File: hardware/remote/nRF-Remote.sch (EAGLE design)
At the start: 26 parts, among them IC1 TP4056, IC2 TPS769XX, J1 62000611121, J2 61300211121, M1 WIRELESS-NRF24L01, SW1 B3F-1000, U1 ATMEGA328P-AU

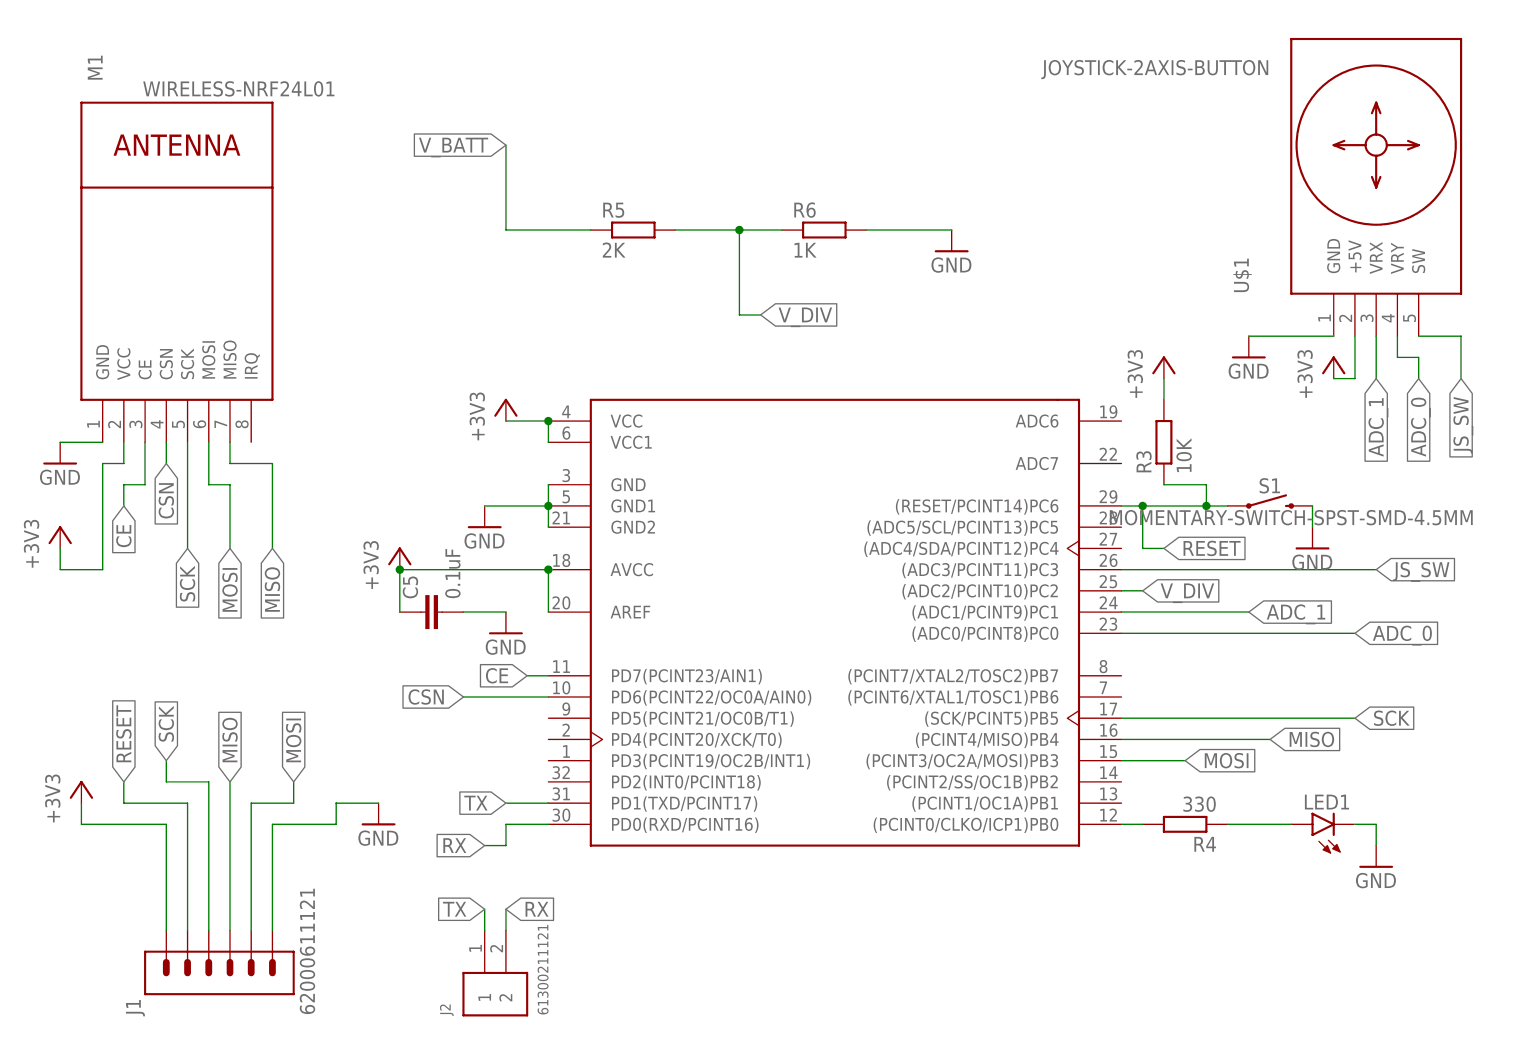
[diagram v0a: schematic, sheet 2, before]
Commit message: Update design with external XTAL, add buttons
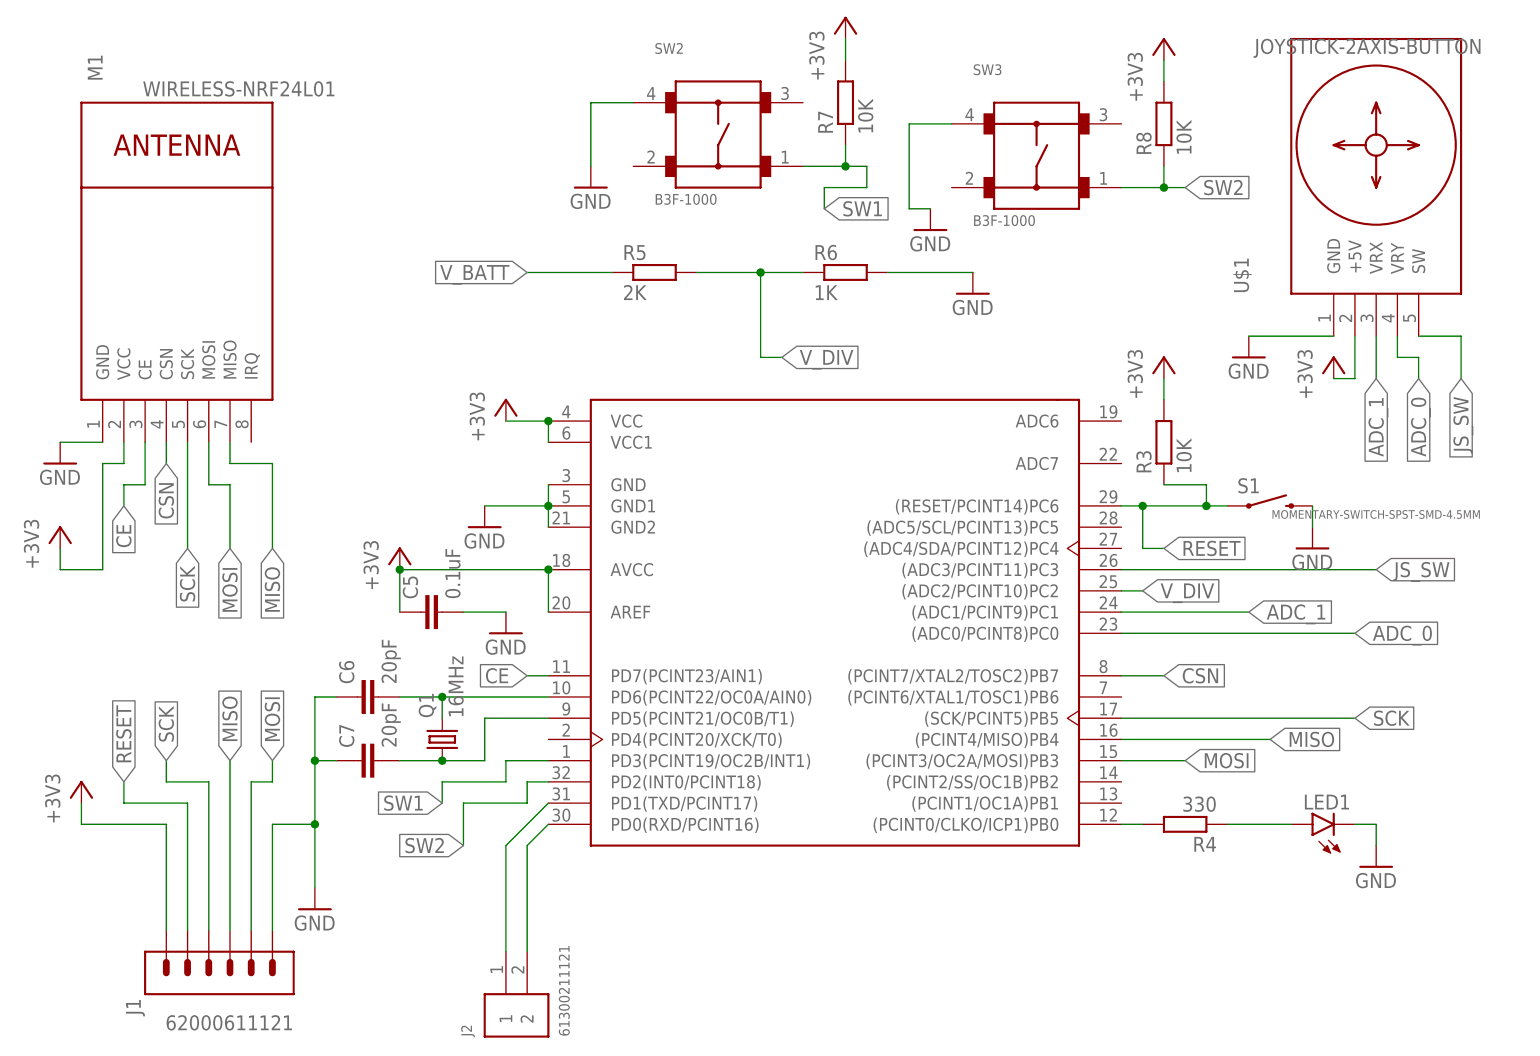
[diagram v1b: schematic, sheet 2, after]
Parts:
- added C6, C7: 20pF, rcl:C-EUC0603
- added Q1: 16MHz, adafruit:CRYSTALSM49
- added R7, R8: 10K, rcl:R-EU_R0603
- added SW2, SW3: B3F-1000, Switch:B3F-1000
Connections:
- net RX renamed N$15
- net TX renamed N$16
- new net N$10: C7.2, Q1.1, U1.PD5(PCINT21/OC0B/T1)
- new net N$8: C6.2, Q1.2, U1.PD6(PCINT22/OC0A/AIN0)
- new net SW1: R7.1, SW2.1, U1.PD3(PCINT19/OC2B/INT1)
- new net SW2: R8.1, SW3.1, U1.PD2(INT0/PCINT18)
- net +3V3: now also R7.2, R8.2
- net CSN: now also U1.(PCINT7/XTAL2/TOSC2)PB7; no longer U1.PD6(PCINT22/OC0A/AIN0)
- net GND: now also C6.1, C7.1, SW2.4, SW3.4
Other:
- moved on the sheet: J2, R5, R6
